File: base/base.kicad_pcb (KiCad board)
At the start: 2 copper layers, 84.3 x 50.8 mm, 30 parts, among them J1 USB_B_Micro, J2 Conn_01x06, SW1 SW_Push_Open, SW2 SW_Push_Open, U1 ESP32-WROOM-32, U2 MCP73831-3-OT, U3 BMP280, U4 TPS63001

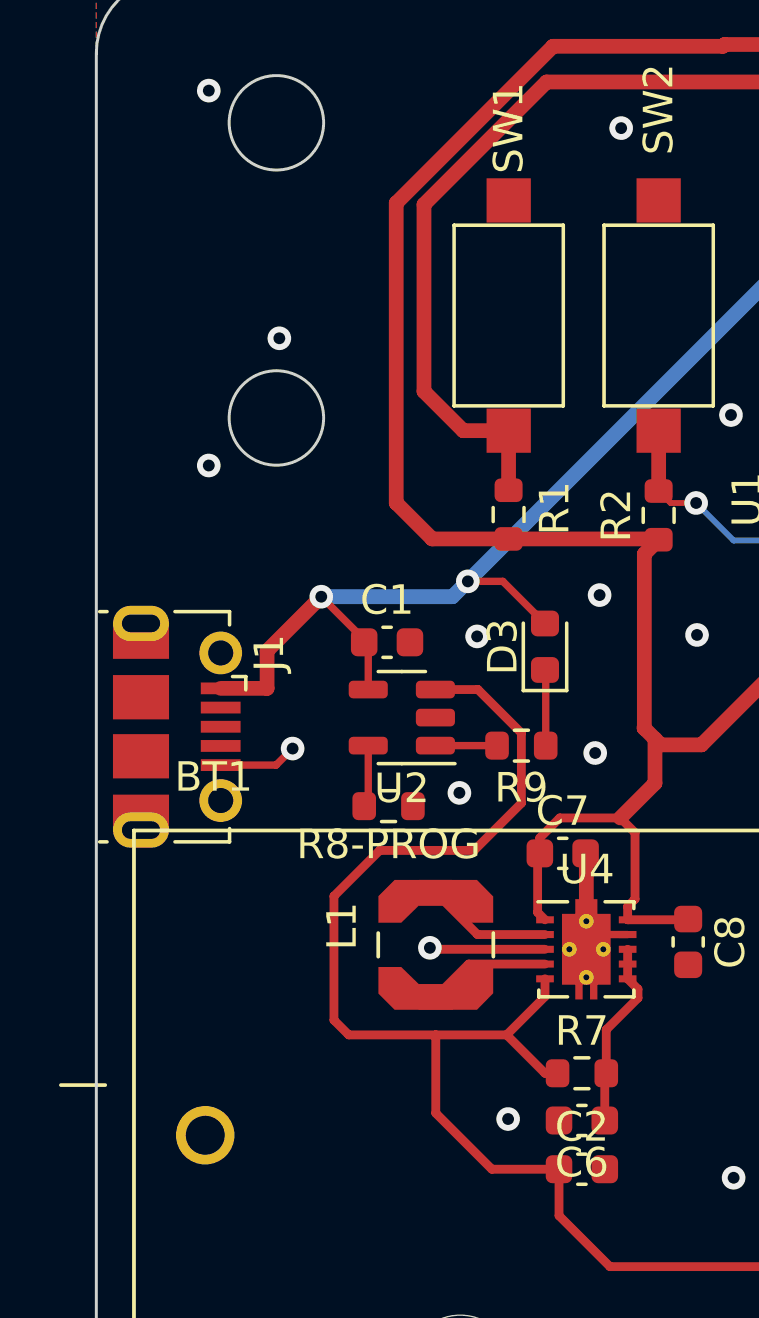
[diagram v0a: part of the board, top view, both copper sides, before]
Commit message: fix battery charging
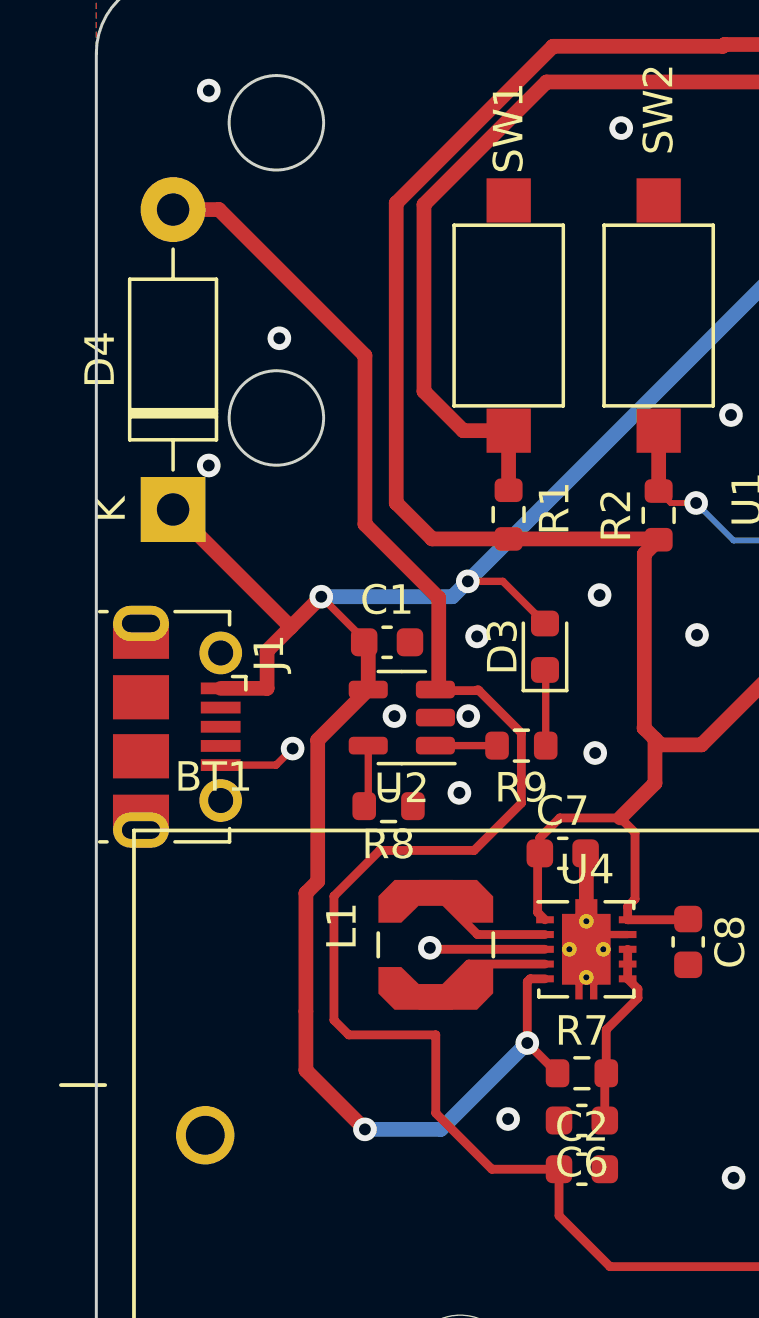
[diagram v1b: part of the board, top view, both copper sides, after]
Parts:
- added D4: 1N4007, Diode_THT:D_DO-41_SOD81_P10.16mm_Horizontal, F.Cu at (91.5, 81.5)
- renumbered R8-PROG to R8
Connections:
- R7 pad 1: BAT+ -> 5V
- U4 pad 5: BAT+ -> 5V
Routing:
- net 5V: track 64.7 -> 97.8 mm, vias 3 -> 5
- net BAT+: track 100.5 -> 114.4 mm
- net GND: vias 28 -> 30

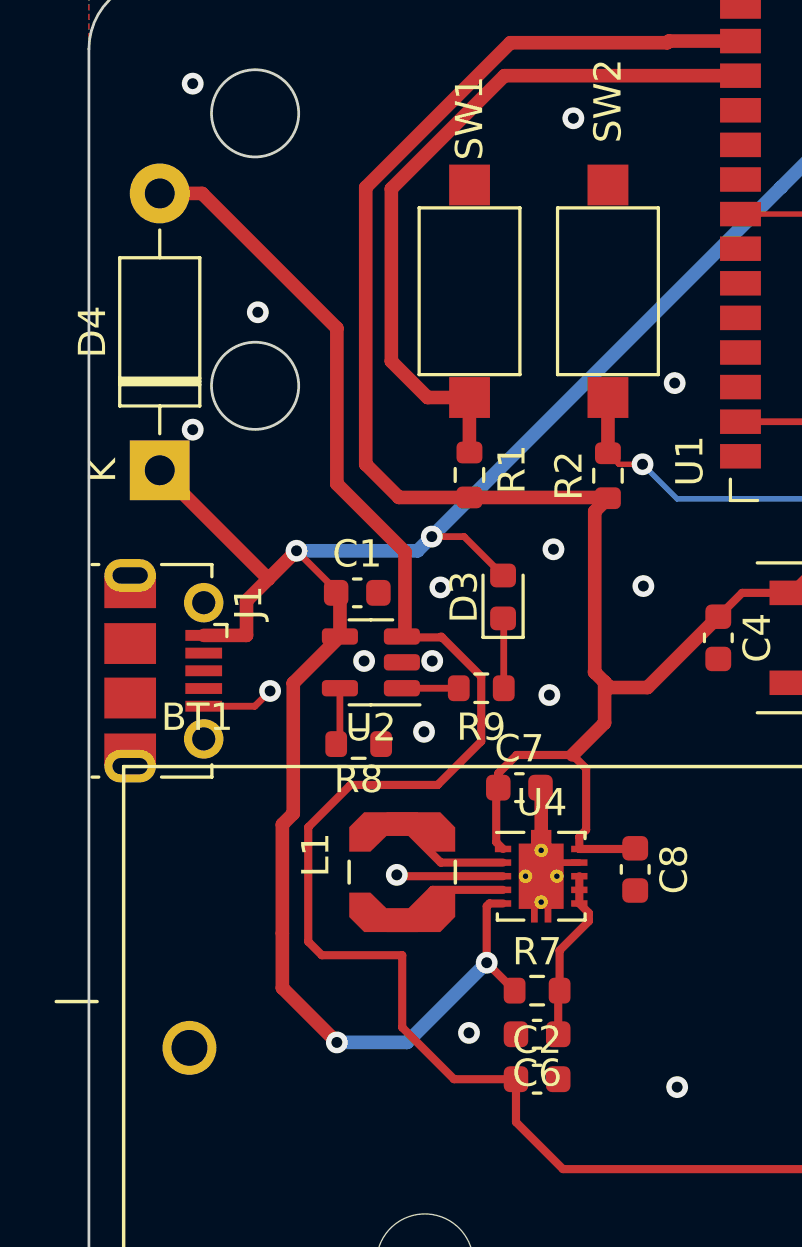
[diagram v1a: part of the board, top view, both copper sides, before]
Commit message: fix battery charging
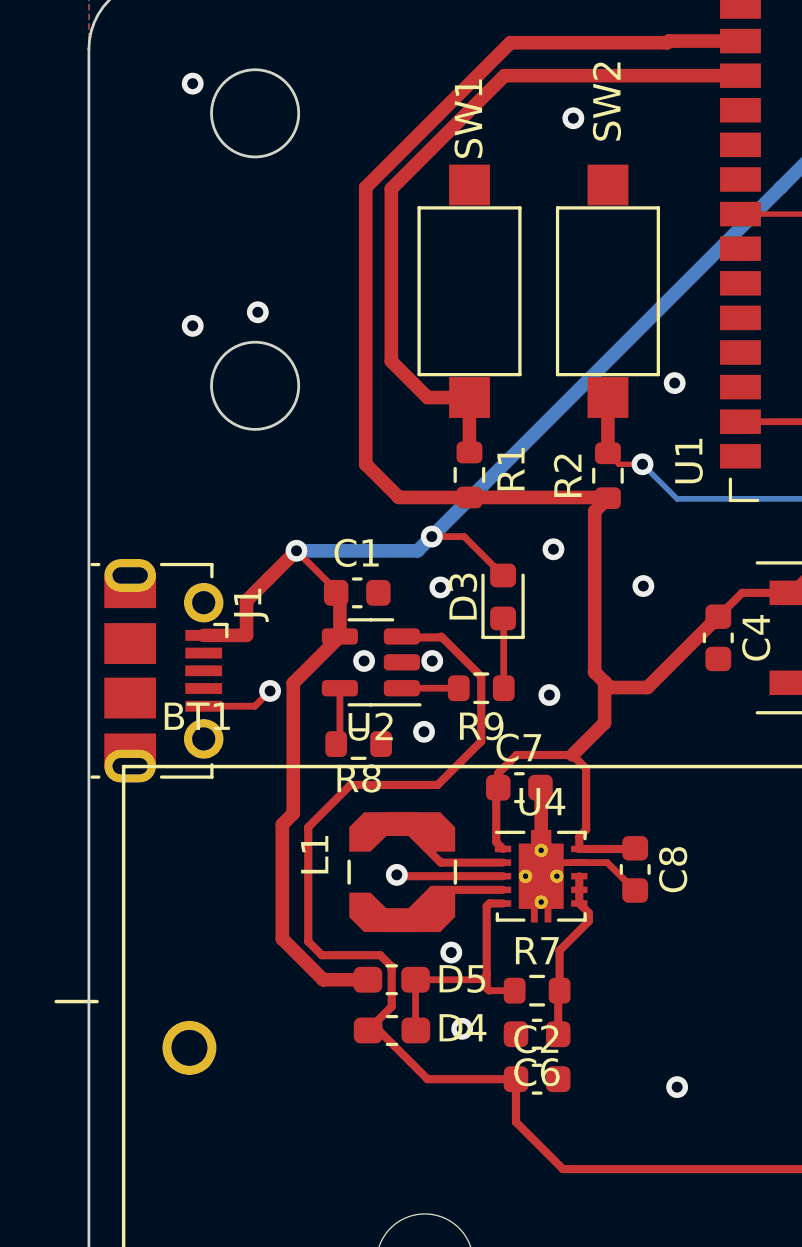
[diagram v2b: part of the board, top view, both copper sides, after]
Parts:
- added D5: 1N4007, Fuse:Fuse_0603_1608Metric_Pad1.05x0.95mm_HandSolder, F.Cu at (100.0, 100.2)
- D4: footprint Diode_THT:D_DO-41_SOD81_P10.16mm_Horizontal -> Fuse:Fuse_0603_1608Metric_Pad1.05x0.95mm_HandSolder
- moved D4 22.3 mm to (100.0, 102.1), turned to 180 degrees
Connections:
- D4 pad 1: 5V -> Net-(D4-K)
- R7 pad 1: 5V -> Net-(D4-K)
- U4 pad 5: 5V -> Net-(D4-K)
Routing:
- net BAT+: track 114.4 -> 94.6 mm
- net 5V: track 97.8 -> 80.5 mm, vias 5 -> 3
- net Net-(D4-K): track 0.00 -> 9.27 mm
- net GND: track 16.3 -> 18.7 mm, vias 30 -> 31

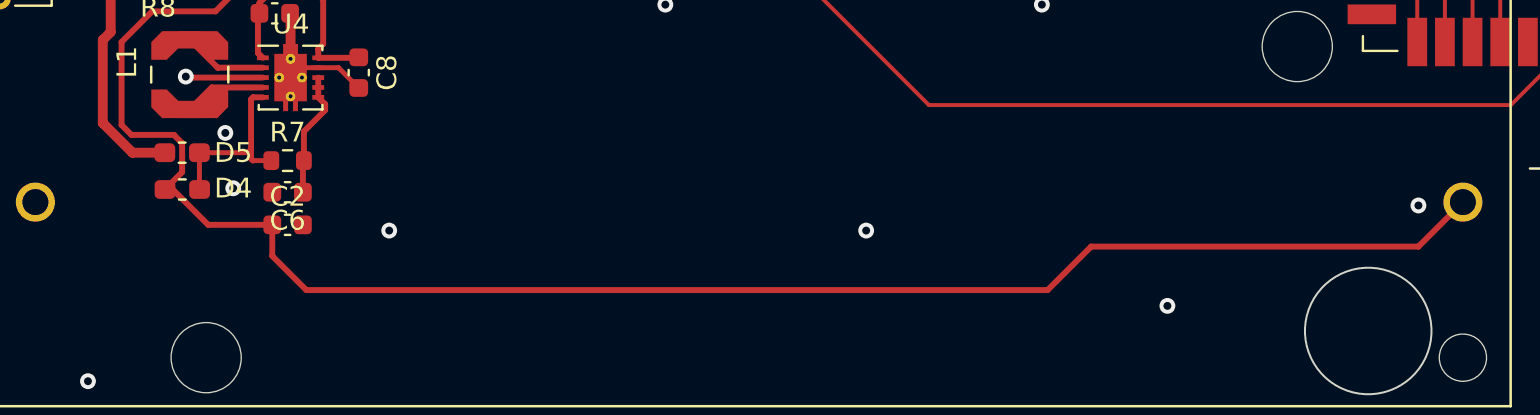
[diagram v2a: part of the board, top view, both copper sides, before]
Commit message: change diode footprint
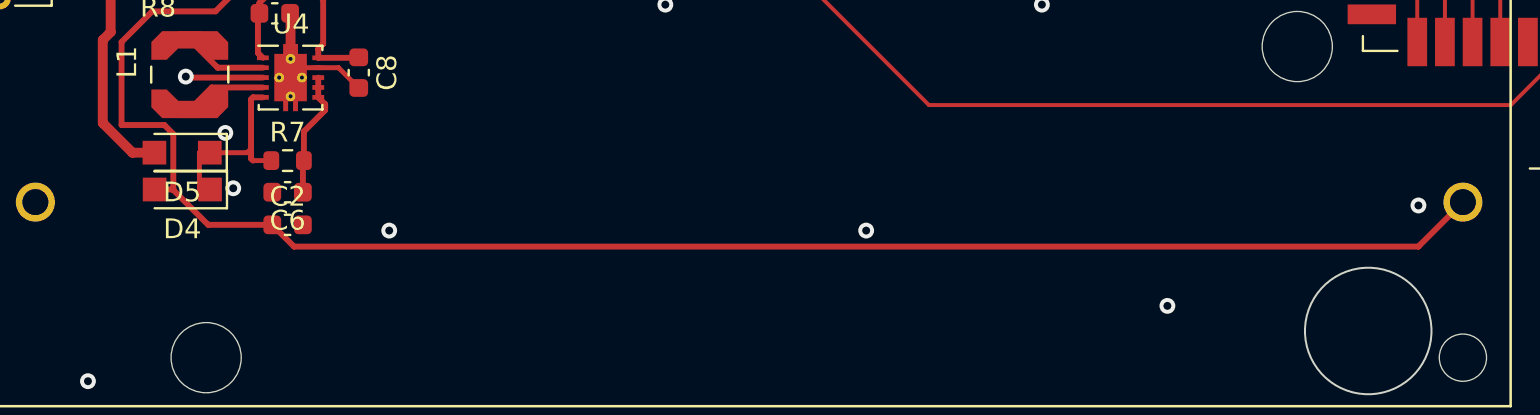
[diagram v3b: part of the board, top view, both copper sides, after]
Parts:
- D4, D5: footprint Fuse:Fuse_0603_1608Metric_Pad1.05x0.95mm_HandSolder -> Diode_SMD:Nexperia_CFP3_SOD-123W
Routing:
- net BAT+: track 94.6 -> 91.7 mm
- net 5V: track 80.5 -> 79.9 mm
